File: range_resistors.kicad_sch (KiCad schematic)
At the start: 8 parts, among them U6 74HC4051

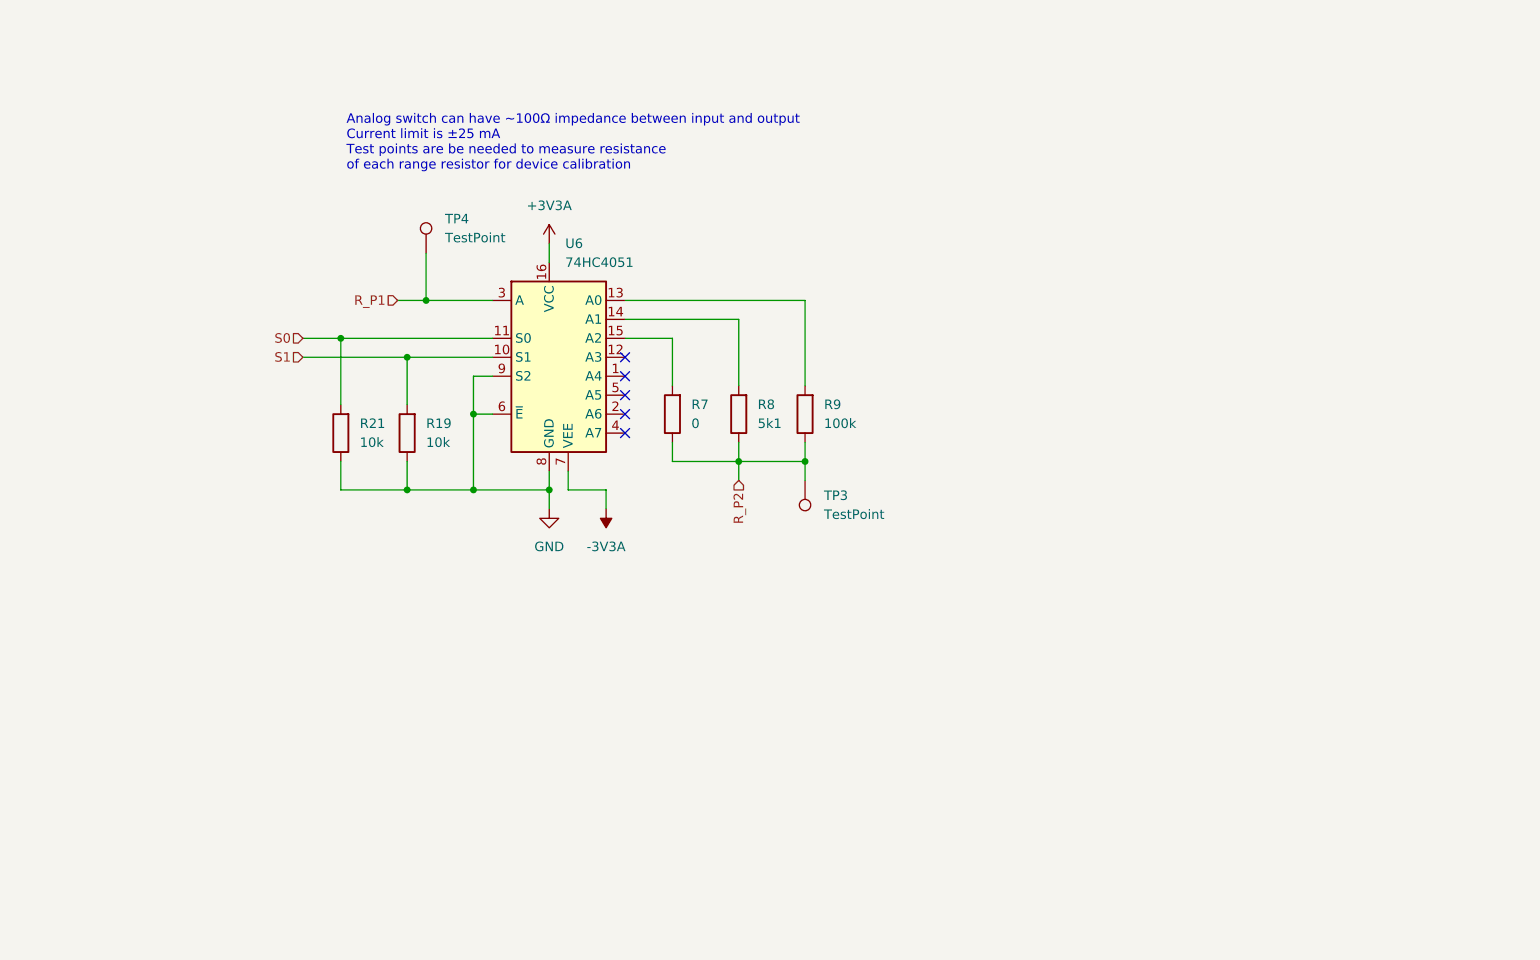
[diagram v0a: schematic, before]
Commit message: Did some routing
Commiting before changing display from i2c to spi
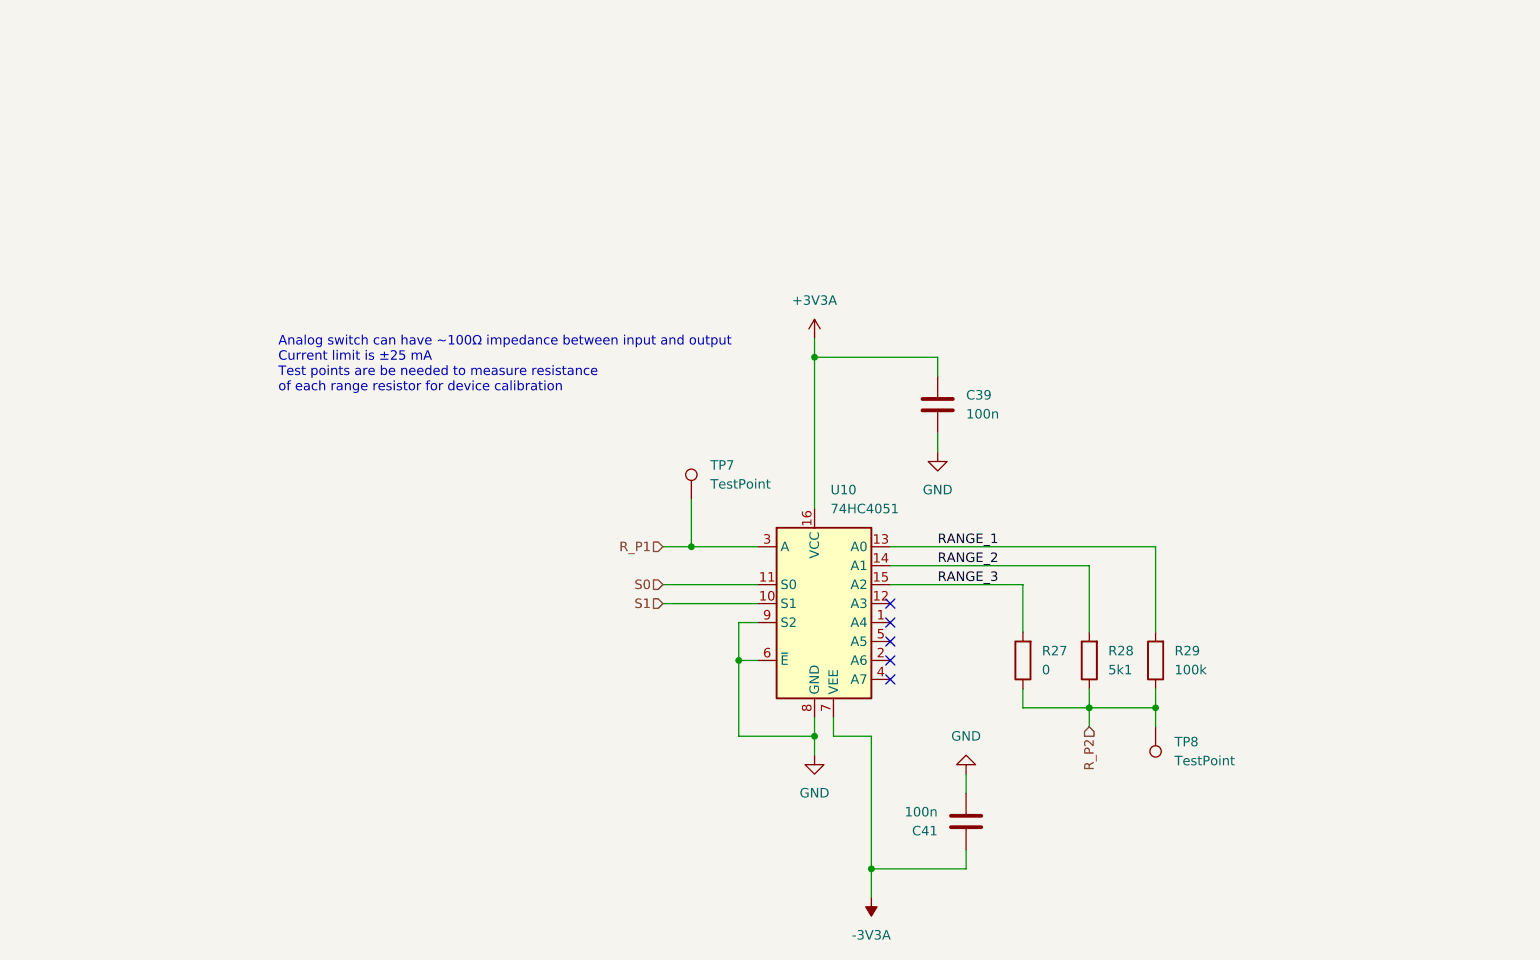
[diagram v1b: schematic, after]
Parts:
- removed R19, R21: 10k, Resistor_SMD:R_0603_1608Metric, symbol Device:R
- added C39, C41: 100n, Capacitor_SMD:C_0603_1608Metric, symbol Device:C
- renumbered R7 to R27, R8 to R28, R9 to R29, TP4 to TP7, TP3 to TP8, U6 to U10
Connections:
- net +3V3A: now also C39.2
- net -3V3A: now also C41.2
- net GND: now also C39.1, C41.1
- net RANGE_2: now reaches R28.2, U10.14 (A1)
- net RANGE_1: now reaches R29.2, U10.13 (A0)
- net RANGE_3: now reaches R27.2, U10.15 (A2)
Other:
- moved on the sheet: R27, R28, R29, TP7, TP8, U10

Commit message: Done
Schematics and PCB are "done".
Meaning I've just finished but need to review
the design before it's ready to order.
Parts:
- renumbered C39 to C40, R27 to R21, R28 to R22, R29 to R23, TP8 to TP10, TP7 to TP9
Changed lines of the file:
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@@
 		(dnp no)
 		(fields_autoplaced yes)
-		(property "Reference" "R28"
+		(property "Reference" "R22"
 			(at 168.91 97.7899 0)
 			(show_name no)
@@
 			(project "lcr"
 				(path "/226ea51e-4da2-4daa-967e-dce167947430/c9f416db-c7a0-48f3-8fda-35fdd9af5fe5/498f4e60-134d-473a-b487-d86df052d229"
-					(reference "R31")
+					(reference "R25")
 					(unit 1)
 				)
 				(path "/226ea51e-4da2-4daa-967e-dce167947430/c9f416db-c7a0-48f3-8fda-35fdd9af5fe5/ec704481-2e23-475c-acd0-894f13851a8c"
-					(reference "R28")
+					(reference "R22")
 					(unit 1)
 				)
@@
 			(project "lcr"
 				(path "/226ea51e-4da2-4daa-967e-dce167947430/c9f416db-c7a0-48f3-8fda-35fdd9af5fe5/498f4e60-134d-473a-b487-d86df052d229"
-					(reference "#PWR090")
+					(reference "#PWR091")
 					(unit 1)
 				)
@@
 		(dnp no)
 		(fields_autoplaced yes)
-		(property "Reference" "#PWR083"
+		(property "Reference" "#PWR082"
 			(at 129.54 59.69 0)
 			(hide yes)
@@
 				)
 				(path "/226ea51e-4da2-4daa-967e-dce167947430/c9f416db-c7a0-48f3-8fda-35fdd9af5fe5/ec704481-2e23-475c-acd0-894f13851a8c"
-					(reference "#PWR083")
+					(reference "#PWR082")
 					(unit 1)
 				)
@@
 		(dnp no)
 		(fields_autoplaced yes)
-		(property "Reference" "C39"
+		(property "Reference" "C40"
 			(at 149.86 63.4999 0)
 			(show_name no)
@@
 			(project "lcr"
 				(path "/226ea51e-4da2-4daa-967e-dce167947430/c9f416db-c7a0-48f3-8fda-35fdd9af5fe5/498f4e60-134d-473a-b487-d86df052d229"
+					(reference "C42")
+					(unit 1)
+				)
+				(path "/226ea51e-4da2-4daa-967e-dce167947430/c9f416db-c7a0-48f3-8fda-35fdd9af5fe5/ec704481-2e23-475c-acd0-894f13851a8c"
 					(reference "C40")
-					(unit 1)
-				)
-				(path "/226ea51e-4da2-4daa-967e-dce167947430/c9f416db-c7a0-48f3-8fda-35fdd9af5fe5/ec704481-2e23-475c-acd0-894f13851a8c"
-					(reference "C39")
 					(unit 1)
 				)
@@
 		(dnp no)
 		(fields_autoplaced yes)
-		(property "Reference" "R27"
+		(property "Reference" "R21"
 			(at 160.02 97.7899 0)
 			(show_name no)
@@
 			(project "lcr"
 				(path "/226ea51e-4da2-4daa-967e-dce167947430/c9f416db-c7a0-48f3-8fda-35fdd9af5fe5/498f4e60-134d-473a-b487-d86df052d229"
-					(reference "R30")
+					(reference "R24")
 					(unit 1)
 				)
 				(path "/226ea51e-4da2-4daa-967e-dce167947430/c9f416db-c7a0-48f3-8fda-35fdd9af5fe5/ec704481-2e23-475c-acd0-894f13851a8c"
-					(reference "R27")
+					(reference "R21")
 					(unit 1)
 				)
@@
 		(dnp no)
 		(fields_autoplaced yes)
-		(property "Reference" "#PWR085"
+		(property "Reference" "#PWR084"
 			(at 129.54 118.11 0)
 			(hide yes)
@@
 				)
 				(path "/226ea51e-4da2-4daa-967e-dce167947430/c9f416db-c7a0-48f3-8fda-35fdd9af5fe5/ec704481-2e23-475c-acd0-894f13851a8c"
-					(reference "#PWR085")
+					(reference "#PWR084")
 					(unit 1)
 				)
@@
 			(project "lcr"
 				(path "/226ea51e-4da2-4daa-967e-dce167947430/c9f416db-c7a0-48f3-8fda-35fdd9af5fe5/498f4e60-134d-473a-b487-d86df052d229"
-					(reference "C42")
+					(reference "C43")
 					(unit 1)
 				)
@@
 		(dnp no)
 		(fields_autoplaced yes)
-		(property "Reference" "TP8"
+		(property "Reference" "TP10"
 			(at 177.8 109.9819 0)
 			(show_name no)
@@
 			(project "lcr"
 				(path "/226ea51e-4da2-4daa-967e-dce167947430/c9f416db-c7a0-48f3-8fda-35fdd9af5fe5/498f4e60-134d-473a-b487-d86df052d229"
+					(reference "TP12")
+					(unit 1)
+				)
+				(path "/226ea51e-4da2-4daa-967e-dce167947430/c9f416db-c7a0-48f3-8fda-35fdd9af5fe5/ec704481-2e23-475c-acd0-894f13851a8c"
 					(reference "TP10")
-					(unit 1)
-				)
-				(path "/226ea51e-4da2-4daa-967e-dce167947430/c9f416db-c7a0-48f3-8fda-35fdd9af5fe5/ec704481-2e23-475c-acd0-894f13851a8c"
-					(reference "TP8")
 					(unit 1)
 				)
@@
 		(dnp no)
 		(fields_autoplaced yes)
-		(property "Reference" "#PWR091"
+		(property "Reference" "#PWR085"
 			(at 149.86 107.95 0)
 			(hide yes)
@@
 			(project "lcr"
 				(path "/226ea51e-4da2-4daa-967e-dce167947430/c9f416db-c7a0-48f3-8fda-35fdd9af5fe5/498f4e60-134d-473a-b487-d86df052d229"
-					(reference "#PWR092")
+					(reference "#PWR090")
 					(unit 1)
 				)
 				(path "/226ea51e-4da2-4daa-967e-dce167947430/c9f416db-c7a0-48f3-8fda-35fdd9af5fe5/ec704481-2e23-475c-acd0-894f13851a8c"
-					(reference "#PWR091")
+					(reference "#PWR085")
 					(unit 1)
 				)
@@
 		(dnp no)
 		(fields_autoplaced yes)
-		(property "Reference" "R29"
+		(property "Reference" "R23"
 			(at 177.8 97.7899 0)
 			(show_name no)
@@
 			(project "lcr"
 				(path "/226ea51e-4da2-4daa-967e-dce167947430/c9f416db-c7a0-48f3-8fda-35fdd9af5fe5/498f4e60-134d-473a-b487-d86df052d229"
-					(reference "R32")
+					(reference "R26")
 					(unit 1)
 				)
 				(path "/226ea51e-4da2-4daa-967e-dce167947430/c9f416db-c7a0-48f3-8fda-35fdd9af5fe5/ec704481-2e23-475c-acd0-894f13851a8c"
-					(reference "R29")
+					(reference "R23")
 					(unit 1)
 				)
@@
 		(dnp no)
 		(fields_autoplaced yes)
-		(property "Reference" "#PWR084"
+		(property "Reference" "#PWR083"
 			(at 146.05 77.47 0)
 			(hide yes)
@@
 				)
 				(path "/226ea51e-4da2-4daa-967e-dce167947430/c9f416db-c7a0-48f3-8fda-35fdd9af5fe5/ec704481-2e23-475c-acd0-894f13851a8c"
-					(reference "#PWR084")
+					(reference "#PWR083")
 					(unit 1)
 				)
@@
 		(dnp no)
 		(fields_autoplaced yes)
-		(property "Reference" "TP7"
+		(property "Reference" "TP9"
 			(at 115.57 72.8979 0)
 			(show_name no)
@@
 			(project "lcr"
 				(path "/226ea51e-4da2-4daa-967e-dce167947430/c9f416db-c7a0-48f3-8fda-35fdd9af5fe5/498f4e60-134d-473a-b487-d86df052d229"
+					(reference "TP11")
+					(unit 1)
+				)
+				(path "/226ea51e-4da2-4daa-967e-dce167947430/c9f416db-c7a0-48f3-8fda-35fdd9af5fe5/ec704481-2e23-475c-acd0-894f13851a8c"
 					(reference "TP9")
 					(unit 1)
 				)
-				(path "/226ea51e-4da2-4daa-967e-dce167947430/c9f416db-c7a0-48f3-8fda-35fdd9af5fe5/ec704481-2e23-475c-acd0-894f13851a8c"
-					(reference "TP7")
-					(unit 1)
-				)

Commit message: Added polish
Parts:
- renumbered R21 to R23, R22 to R24, R23 to R25, TP9 to TP11, TP10 to TP12
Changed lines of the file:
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@@
 		(dnp no)
 		(fields_autoplaced yes)
-		(property "Reference" "R22"
+		(property "Reference" "R24"
 			(at 168.91 97.7899 0)
 			(show_name no)
@@
 			(project "lcr"
 				(path "/226ea51e-4da2-4daa-967e-dce167947430/c9f416db-c7a0-48f3-8fda-35fdd9af5fe5/498f4e60-134d-473a-b487-d86df052d229"
-					(reference "R25")
+					(reference "R27")
 					(unit 1)
 				)
 				(path "/226ea51e-4da2-4daa-967e-dce167947430/c9f416db-c7a0-48f3-8fda-35fdd9af5fe5/ec704481-2e23-475c-acd0-894f13851a8c"
-					(reference "R22")
+					(reference "R24")
 					(unit 1)
 				)
@@
 		(dnp no)
 		(fields_autoplaced yes)
-		(property "Reference" "#PWR086"
+		(property "Reference" "#PWR092"
 			(at 137.16 127 0)
 			(hide yes)
@@
 			(project "lcr"
 				(path "/226ea51e-4da2-4daa-967e-dce167947430/c9f416db-c7a0-48f3-8fda-35fdd9af5fe5/498f4e60-134d-473a-b487-d86df052d229"
-					(reference "#PWR091")
+					(reference "#PWR097")
 					(unit 1)
 				)
 				(path "/226ea51e-4da2-4daa-967e-dce167947430/c9f416db-c7a0-48f3-8fda-35fdd9af5fe5/ec704481-2e23-475c-acd0-894f13851a8c"
-					(reference "#PWR086")
+					(reference "#PWR092")
 					(unit 1)
 				)
@@
 		(dnp no)
 		(fields_autoplaced yes)
-		(property "Reference" "#PWR082"
+		(property "Reference" "#PWR088"
 			(at 129.54 59.69 0)
 			(hide yes)
@@
 			(project "lcr"
 				(path "/226ea51e-4da2-4daa-967e-dce167947430/c9f416db-c7a0-48f3-8fda-35fdd9af5fe5/498f4e60-134d-473a-b487-d86df052d229"
-					(reference "#PWR087")
+					(reference "#PWR093")
 					(unit 1)
 				)
 				(path "/226ea51e-4da2-4daa-967e-dce167947430/c9f416db-c7a0-48f3-8fda-35fdd9af5fe5/ec704481-2e23-475c-acd0-894f13851a8c"
-					(reference "#PWR082")
+					(reference "#PWR088")
 					(unit 1)
 				)
@@
 		(dnp no)
 		(fields_autoplaced yes)
-		(property "Reference" "R21"
+		(property "Reference" "R23"
 			(at 160.02 97.7899 0)
 			(show_name no)
@@
 			(project "lcr"
 				(path "/226ea51e-4da2-4daa-967e-dce167947430/c9f416db-c7a0-48f3-8fda-35fdd9af5fe5/498f4e60-134d-473a-b487-d86df052d229"
-					(reference "R24")
+					(reference "R26")
 					(unit 1)
 				)
 				(path "/226ea51e-4da2-4daa-967e-dce167947430/c9f416db-c7a0-48f3-8fda-35fdd9af5fe5/ec704481-2e23-475c-acd0-894f13851a8c"
-					(reference "R21")
+					(reference "R23")
 					(unit 1)
 				)
@@
 		(dnp no)
 		(fields_autoplaced yes)
-		(property "Reference" "#PWR084"
+		(property "Reference" "#PWR090"
 			(at 129.54 118.11 0)
 			(hide yes)
@@
 			(project "lcr"
 				(path "/226ea51e-4da2-4daa-967e-dce167947430/c9f416db-c7a0-48f3-8fda-35fdd9af5fe5/498f4e60-134d-473a-b487-d86df052d229"
-					(reference "#PWR089")
+					(reference "#PWR095")
 					(unit 1)
 				)
 				(path "/226ea51e-4da2-4daa-967e-dce167947430/c9f416db-c7a0-48f3-8fda-35fdd9af5fe5/ec704481-2e23-475c-acd0-894f13851a8c"
-					(reference "#PWR084")
+					(reference "#PWR090")
 					(unit 1)
 				)
@@
 		(dnp no)
 		(fields_autoplaced yes)
-		(property "Reference" "TP10"
+		(property "Reference" "TP12"
 			(at 177.8 109.9819 0)
 			(show_name no)
@@
 			(project "lcr"
 				(path "/226ea51e-4da2-4daa-967e-dce167947430/c9f416db-c7a0-48f3-8fda-35fdd9af5fe5/498f4e60-134d-473a-b487-d86df052d229"
+					(reference "TP14")
+					(unit 1)
+				)
+				(path "/226ea51e-4da2-4daa-967e-dce167947430/c9f416db-c7a0-48f3-8fda-35fdd9af5fe5/ec704481-2e23-475c-acd0-894f13851a8c"
 					(reference "TP12")
-					(unit 1)
-				)
-				(path "/226ea51e-4da2-4daa-967e-dce167947430/c9f416db-c7a0-48f3-8fda-35fdd9af5fe5/ec704481-2e23-475c-acd0-894f13851a8c"
-					(reference "TP10")
 					(unit 1)
 				)
@@
 		(dnp no)
 		(fields_autoplaced yes)
-		(property "Reference" "#PWR085"
+		(property "Reference" "#PWR091"
 			(at 149.86 107.95 0)
 			(hide yes)
@@
 			(project "lcr"
 				(path "/226ea51e-4da2-4daa-967e-dce167947430/c9f416db-c7a0-48f3-8fda-35fdd9af5fe5/498f4e60-134d-473a-b487-d86df052d229"
-					(reference "#PWR090")
+					(reference "#PWR096")
 					(unit 1)
 				)
 				(path "/226ea51e-4da2-4daa-967e-dce167947430/c9f416db-c7a0-48f3-8fda-35fdd9af5fe5/ec704481-2e23-475c-acd0-894f13851a8c"
-					(reference "#PWR085")
+					(reference "#PWR091")
 					(unit 1)
 				)
@@
 		(dnp no)
 		(fields_autoplaced yes)
-		(property "Reference" "R23"
+		(property "Reference" "R25"
 			(at 177.8 97.7899 0)
 			(show_name no)
@@
 			(project "lcr"
 				(path "/226ea51e-4da2-4daa-967e-dce167947430/c9f416db-c7a0-48f3-8fda-35fdd9af5fe5/498f4e60-134d-473a-b487-d86df052d229"
-					(reference "R26")
+					(reference "R28")
 					(unit 1)
 				)
 				(path "/226ea51e-4da2-4daa-967e-dce167947430/c9f416db-c7a0-48f3-8fda-35fdd9af5fe5/ec704481-2e23-475c-acd0-894f13851a8c"
-					(reference "R23")
+					(reference "R25")
 					(unit 1)
 				)
@@
 		(dnp no)
 		(fields_autoplaced yes)
-		(property "Reference" "#PWR083"
+		(property "Reference" "#PWR089"
 			(at 146.05 77.47 0)
 			(hide yes)
@@
 			(project "lcr"
 				(path "/226ea51e-4da2-4daa-967e-dce167947430/c9f416db-c7a0-48f3-8fda-35fdd9af5fe5/498f4e60-134d-473a-b487-d86df052d229"
-					(reference "#PWR088")
+					(reference "#PWR094")
 					(unit 1)
 				)
 				(path "/226ea51e-4da2-4daa-967e-dce167947430/c9f416db-c7a0-48f3-8fda-35fdd9af5fe5/ec704481-2e23-475c-acd0-894f13851a8c"
-					(reference "#PWR083")
+					(reference "#PWR089")
 					(unit 1)
 				)
@@
 		(dnp no)
 		(fields_autoplaced yes)
-		(property "Reference" "TP9"
+		(property "Reference" "TP11"
 			(at 115.57 72.8979 0)
 			(show_name no)
@@
 			(project "lcr"
 				(path "/226ea51e-4da2-4daa-967e-dce167947430/c9f416db-c7a0-48f3-8fda-35fdd9af5fe5/498f4e60-134d-473a-b487-d86df052d229"
+					(reference "TP13")
+					(unit 1)
+				)
+				(path "/226ea51e-4da2-4daa-967e-dce167947430/c9f416db-c7a0-48f3-8fda-35fdd9af5fe5/ec704481-2e23-475c-acd0-894f13851a8c"
 					(reference "TP11")
 					(unit 1)
 				)
-				(path "/226ea51e-4da2-4daa-967e-dce167947430/c9f416db-c7a0-48f3-8fda-35fdd9af5fe5/ec704481-2e23-475c-acd0-894f13851a8c"
-					(reference "TP9")
-					(unit 1)
-				)
